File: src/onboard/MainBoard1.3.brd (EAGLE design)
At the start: 134.6 x 80.5 mm, 86 parts, among them IC1 MIC29310-5.0BT, IC3 A5975D, U1 ADAFRUIT_BMP280_BAROMETER

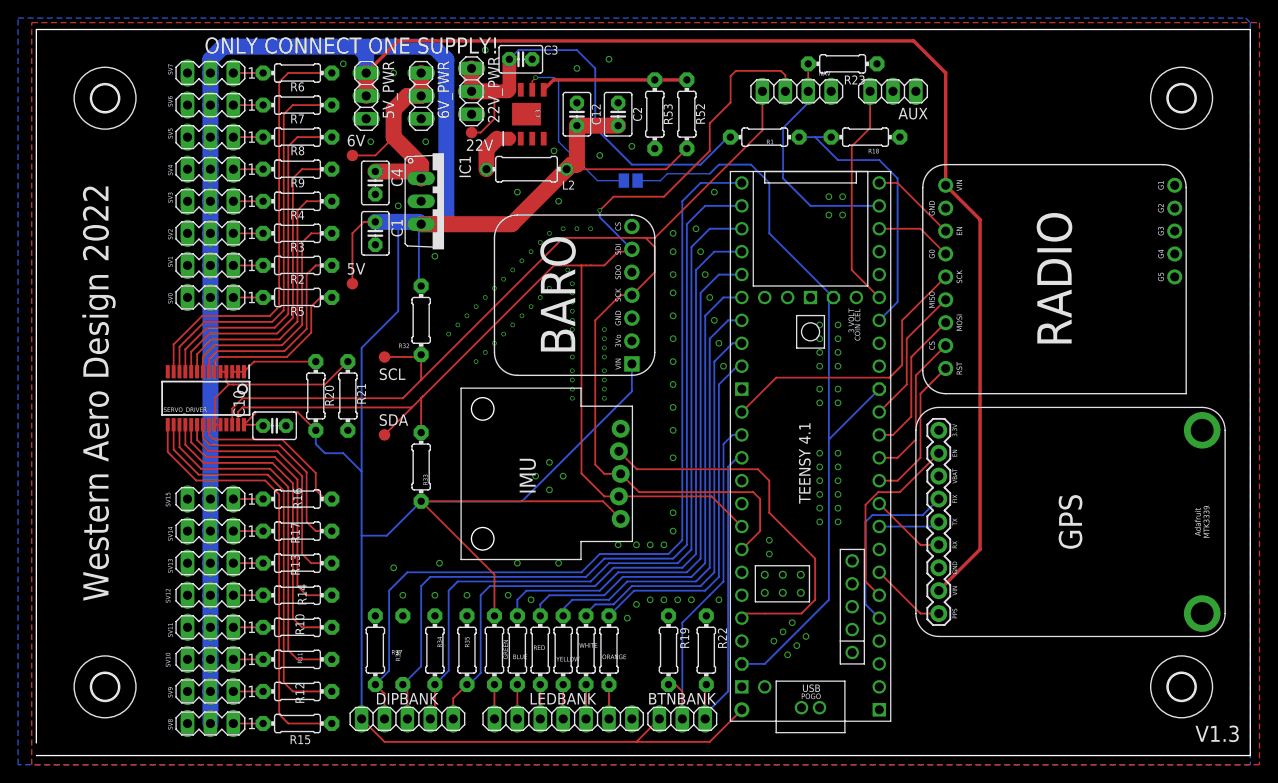
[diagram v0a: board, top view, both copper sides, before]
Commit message: Renamed main board files
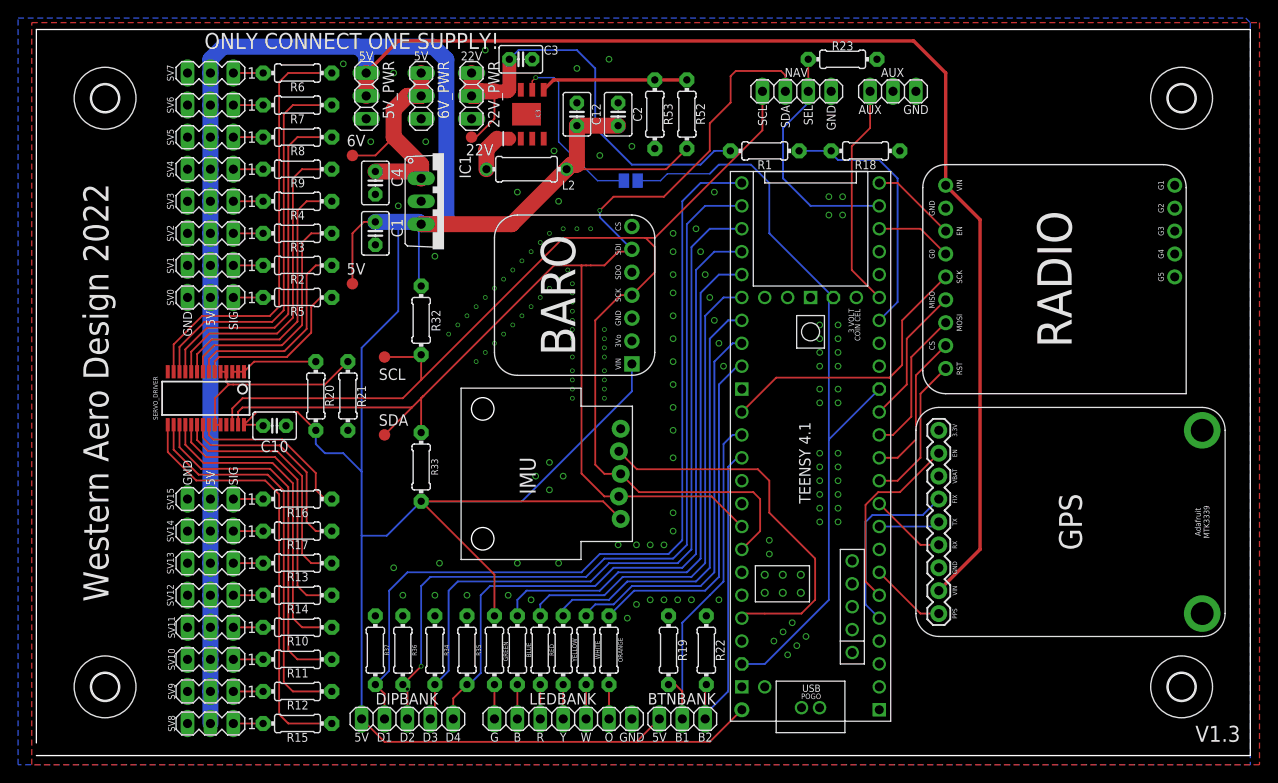
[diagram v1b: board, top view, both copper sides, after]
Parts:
- moved R1 1.52 mm to (80.8, 67.1)
- moved R18 1.52 mm to (91.9, 67.1)
- moved 22V 0.51 mm to (48.3, 68.6)
- moved 22V_PWR 0.51 mm to (48.3, 73.2)
- moved R23 0.51 mm to (89.4, 77.2)
- flipped R36 to the top
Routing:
- net BATLEVEL: track 31.2 -> 28.9 mm
- net SELECT_PIN: track 25.8 -> 26.3 mm
- net DIP2: vias 0 -> 2
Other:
- board text added: "22V"
- board text added: "5V"
- board text added: "AUX"
- board text added: "B"
- board text added: "B1"
- board text added: "B2"
- board text added: "D1"
- board text added: "D2"
- board text added: "D3"
- board text added: "D4"
- board text added: "G"
- board text added: "GND"
- board text added: "O"
- board text added: "R"
- board text added: "SCL"
- board text added: "SDA"
- board text added: "SEL"
- board text added: "SIG"
- board text added: "W"
- board text added: "Y"

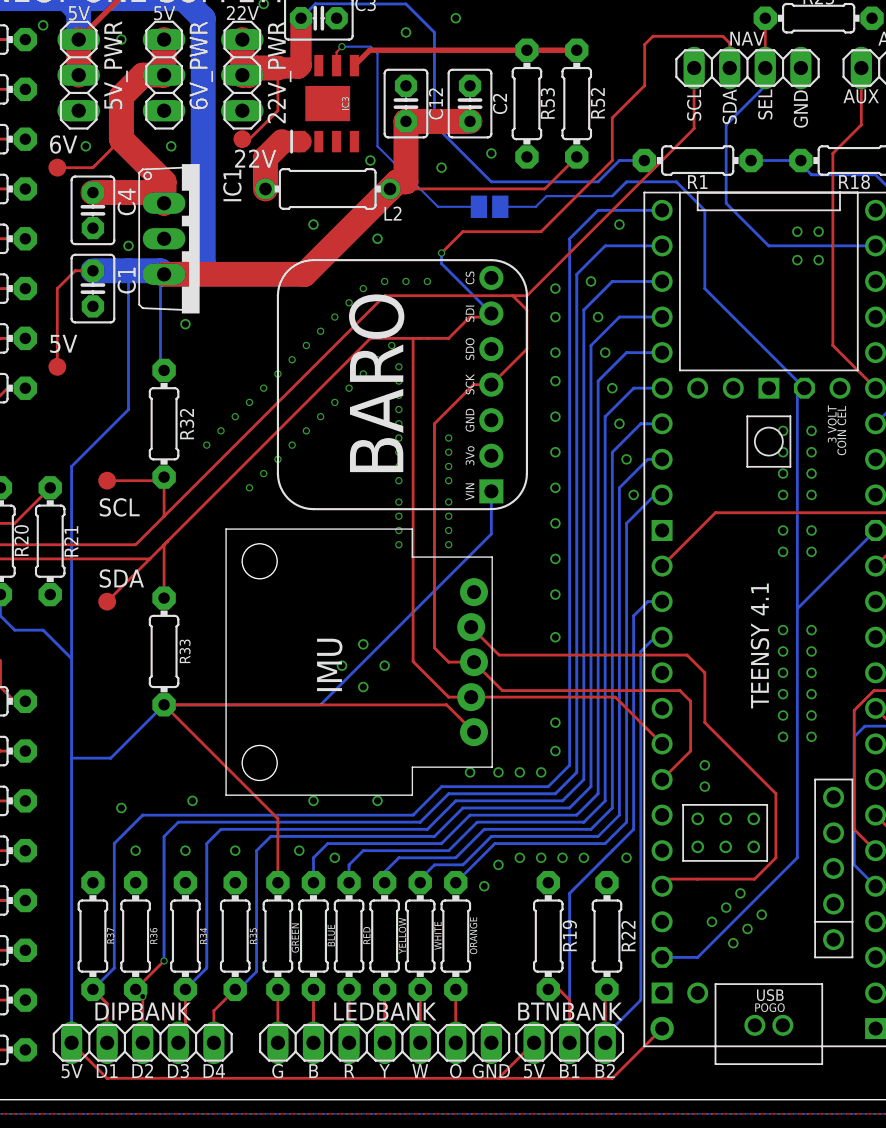
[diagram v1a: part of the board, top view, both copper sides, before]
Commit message: Added gnd test point
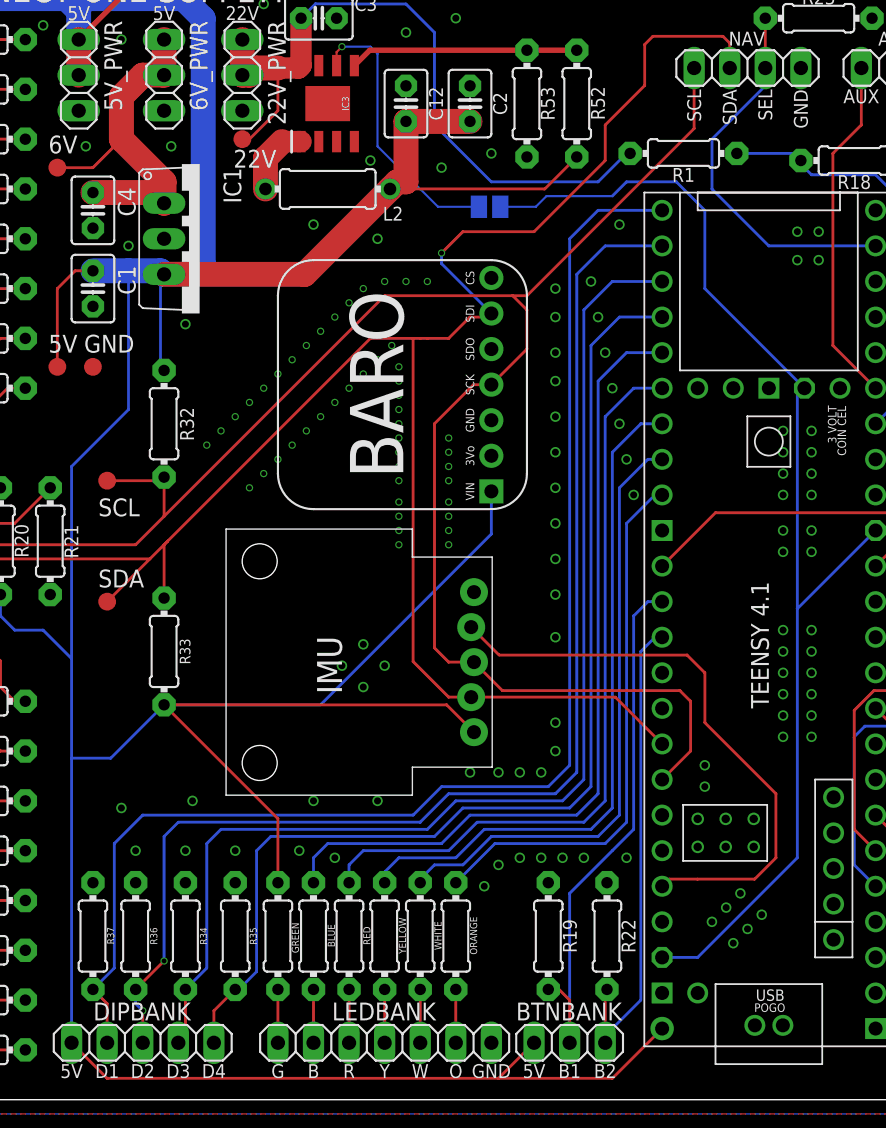
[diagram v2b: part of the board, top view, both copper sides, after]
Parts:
- added GND: PTR1B1,27, testpad:B1,27
- moved R1 1.14 mm to (79.8, 67.6)
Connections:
- net GND: now also GND.TP
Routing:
- net BATLEVEL: track 28.9 -> 30.1 mm
- net SELECT_PIN: track 26.3 -> 27.1 mm
- net 22V_INPUT: track 51.5 -> 50.7 mm
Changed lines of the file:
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@@
 <attribute name="VALUE" x="56.261" y="76.708" size="0.9906" layer="27" ratio="10" align="center-left"/>
 </element>
-<element name="R1" library="adafruit" library_urn="urn:adsk.eagle:library:420" package="0204/7" package3d_urn="urn:adsk.eagle:package:6240596/1" value="1.8M" x="80.772" y="67.056" smashed="yes" rot="R180">
-<attribute name="NAME" x="80.772" y="66.0146" size="0.9906" layer="25" ratio="12" rot="R180" align="bottom-center"/>
-<attribute name="VALUE" x="80.7466" y="67.0306" size="0.9906" layer="27" ratio="12" rot="R180" align="center"/>
+<element name="R1" library="adafruit" library_urn="urn:adsk.eagle:library:420" package="0204/7" package3d_urn="urn:adsk.eagle:package:6240596/1" value="1.8M" x="79.756" y="67.564" smashed="yes" rot="R180">
+<attribute name="NAME" x="79.756" y="66.5226" size="0.9906" layer="25" ratio="12" rot="R180" align="bottom-center"/>
+<attribute name="VALUE" x="79.7306" y="67.5386" size="0.9906" layer="27" ratio="12" rot="R180" align="center"/>
 </element>
 <element name="R18" library="adafruit" library_urn="urn:adsk.eagle:library:420" package="0204/7" package3d_urn="urn:adsk.eagle:package:6240596/1" value="430k" x="91.948" y="67.056" smashed="yes" rot="R180">
@@
 <attribute name="POPULARITY" value="33" x="65.913" y="63.754" size="1.778" layer="28" rot="MR180" display="off"/>
 <attribute name="VALUE" x="66.3131" y="63.754" size="0.02" layer="28" rot="MR180"/>
+</element>
+<element name="GND" library="testpad" library_urn="urn:adsk.eagle:library:385" package="B1,27" package3d_urn="urn:adsk.eagle:package:27944/2" value="PTR1B1,27" x="37.592" y="52.324" smashed="yes">
+<attribute name="NAME" x="36.957" y="53.34" size="1.27" layer="25" ratio="10"/>
+<attribute name="POPULARITY" value="2" x="37.592" y="52.324" size="1.778" layer="27" display="off"/>
+<attribute name="TP_SIGNAL_NAME" value="" x="37.592" y="52.324" size="1.778" layer="27" display="off"/>
+<attribute name="VALUE" x="36.957" y="51.562" size="0.0254" layer="27"/>
 </element>
 </elements>
@@
 <wire x1="82.5754" y1="75.9206" x2="77.567675" y2="75.9206" width="0.2032" layer="1"/>
 <wire x1="76.9874" y1="75.340325" x2="76.9874" y2="72.4154" width="0.2032" layer="1"/>
-<wire x1="74.676" y1="70.104" x2="74.676" y2="67.056" width="0.2032" layer="1"/>
-<wire x1="74.676" y1="67.056" x2="69.596" y2="61.976" width="0.2032" layer="1"/>
+<wire x1="74.168" y1="69.596" x2="74.168" y2="67.056" width="0.2032" layer="1"/>
+<wire x1="74.168" y1="67.056" x2="69.088" y2="61.976" width="0.2032" layer="1"/>
 <wire x1="64.008" y1="61.976" x2="62.484" y2="60.452" width="0.2032" layer="1"/>
 <via x="62.484" y="60.452" extent="1-16" drill="0.35"/>
 <wire x1="62.484" y1="60.452" x2="62.484" y2="59.69" width="0.2032" layer="16"/>
 <wire x1="62.484" y1="59.69" x2="66.04" y2="56.134" width="0.2032" layer="16"/>
-<wire x1="76.9874" y1="72.4154" x2="74.676" y2="70.104" width="0.2032" layer="1"/>
-<wire x1="69.596" y1="61.976" x2="64.008" y2="61.976" width="0.2032" layer="1"/>
+<wire x1="76.9874" y1="72.4154" x2="74.168" y2="69.596" width="0.2032" layer="1"/>
+<wire x1="69.088" y1="61.976" x2="64.008" y2="61.976" width="0.2032" layer="1"/>
 <wire x1="64.599" y1="28.742" x2="62.992" y2="28.742" width="0.2032" layer="1"/>
 <wire x1="62.992" y1="28.742" x2="60.452" y2="31.282" width="0.2032" layer="1"/>
@@
 <contactref element="R36" pad="2"/>
 <contactref element="DIPBANK" pad="3"/>
-<wire x1="40.64" y1="7.874" x2="41.148" y2="7.366" width="0.2032" layer="16"/>
-<wire x1="41.148" y1="7.366" x2="41.148" y2="4.064" width="0.2032" layer="1"/>
+<wire x1="40.64" y1="7.874" x2="40.64" y2="6.858" width="0.2032" layer="16"/>
+<wire x1="41.148" y1="6.35" x2="40.64" y2="6.858" width="0.2032" layer="16"/>
+<wire x1="41.148" y1="6.35" x2="41.148" y2="4.064" width="0.2032" layer="1"/>
 <wire x1="74.168" y1="60.96" x2="72.136" y2="58.928" width="0.2032" layer="16"/>
 <wire x1="78.232" y1="60.96" x2="74.168" y2="60.96" width="0.2032" layer="16"/>
@@
 <wire x1="42.672" y1="9.906" x2="40.64" y2="7.874" width="0.2032" layer="1"/>
 <wire x1="42.672" y1="18.796" x2="42.672" y2="9.906" width="0.2032" layer="16"/>
-<via x="41.148" y="7.366" extent="1-16" drill="0.35"/>
+<via x="41.148" y="6.35" extent="1-16" drill="0.35"/>
 <via x="42.672" y="9.906" extent="1-16" drill="0.35"/>
 </signal>
@@
 <via x="44.196" y="55.372" extent="1-16" drill="0.5"/>
 <via x="34.036" y="76.708" extent="1-16" drill="0.5"/>
+<contactref element="GND" pad="TP"/>
 </signal>
 <signal name="GPS_EN">
@@
 <contactref element="TEENSY4.1" pad="31-CTX3"/>
 <wire x1="85.598" y1="73.66" x2="85.598" y2="72.39" width="0.2032" layer="16"/>
-<wire x1="85.598" y1="72.39" x2="82.804" y2="69.596" width="0.2032" layer="16"/>
-<wire x1="82.804" y1="69.596" x2="82.804" y2="64.008" width="0.2032" layer="16"/>
+<wire x1="85.598" y1="72.39" x2="81.788" y2="68.58" width="0.2032" layer="16"/>
+<wire x1="81.788" y1="68.58" x2="81.788" y2="65.024" width="0.2032" layer="16"/>
 <wire x1="85.852" y1="60.96" x2="93.472" y2="60.96" width="0.2032" layer="16"/>
-<wire x1="82.804" y1="64.008" x2="85.852" y2="60.96" width="0.2032" layer="16"/>
+<wire x1="81.788" y1="65.024" x2="85.852" y2="60.96" width="0.2032" layer="16"/>
 <wire x1="85.598" y1="77.216" x2="85.598" y2="73.66" width="0.2032" layer="1"/>
 </signal>
@@
 <wire x1="88.9" y1="66.04" x2="88.138" y2="66.802" width="0.2032" layer="16"/>
 <wire x1="88.138" y1="66.802" x2="88.138" y2="67.056" width="0.2032" layer="16"/>
-<wire x1="84.582" y1="67.056" x2="88.138" y2="67.056" width="0.2032" layer="16"/>
+<wire x1="87.63" y1="67.564" x2="83.566" y2="67.564" width="0.2032" layer="16"/>
+<wire x1="87.63" y1="67.564" x2="88.138" y2="67.056" width="0.2032" layer="16"/>
 </signal>
 <signal name="MISO0">
@@
 <wire x1="66.04" y1="65.532" x2="73.66" y2="65.532" width="0.2032" layer="16"/>
 <contactref element="R1" pad="2"/>
-<wire x1="76.962" y1="67.056" x2="75.184" y2="67.056" width="0.2032" layer="16"/>
-<wire x1="75.184" y1="67.056" x2="73.66" y2="65.532" width="0.2032" layer="16"/>
+<wire x1="75.946" y1="67.564" x2="75.692" y2="67.564" width="0.2032" layer="16"/>
+<wire x1="75.692" y1="67.564" x2="73.66" y2="65.532" width="0.2032" layer="16"/>
 <wire x1="48.26" y1="68.58" x2="48.768" y2="68.58" width="0.2032" layer="1"/>
 <wire x1="48.768" y1="68.58" x2="50.8" y2="70.612" width="0.2032" layer="1"/>

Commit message: Performed ERC and made changes
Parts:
- 22V_PWR: value (none) -> 22V_PWR
- 5V_PWR: value (none) -> 5V_PWR
- 6V_PWR: value (none) -> 6V_PWR
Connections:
- removed net AUX_DATA: TEENSY4.1.6-OUT1D
- removed net N$4: AUX.2
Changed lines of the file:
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@@
 <attribute name="VALUE" x="47.498" y="7.239" size="1.27" layer="27" rot="R180"/>
 </element>
-<element name="6V_PWR" library="pinhead" library_urn="urn:adsk.eagle:library:325" package="1X03" package3d_urn="urn:adsk.eagle:package:22458/2" value="" x="42.672" y="73.152" smashed="yes" rot="R270">
+<element name="6V_PWR" library="pinhead" library_urn="urn:adsk.eagle:library:325" package="1X03" package3d_urn="urn:adsk.eagle:package:22458/2" value="6V_PWR" x="42.672" y="73.152" smashed="yes" rot="R270">
 <attribute name="NAME" x="44.5008" y="77.0382" size="1.27" layer="25" ratio="10" rot="R270"/>
 <attribute name="POPULARITY" value="92" x="42.672" y="73.152" size="1.778" layer="27" rot="R270" display="off"/>
-<attribute name="VALUE" x="39.497" y="76.962" size="1.27" layer="27" rot="R270"/>
 </element>
 <element name="LEDBANK" library="pinhead" library_urn="urn:adsk.eagle:library:325" package="1X07" package3d_urn="urn:adsk.eagle:package:22477/2" value="" x="58.42" y="4.064" smashed="yes" rot="R180">
@@
 <attribute name="VALUE" x="67.31" y="7.239" size="1.27" layer="27" rot="R180"/>
 </element>
-<element name="22V_PWR" library="pinhead" library_urn="urn:adsk.eagle:library:325" package="1X03" package3d_urn="urn:adsk.eagle:package:22458/2" value="" x="48.26" y="73.152" smashed="yes" rot="R270">
+<element name="22V_PWR" library="pinhead" library_urn="urn:adsk.eagle:library:325" package="1X03" package3d_urn="urn:adsk.eagle:package:22458/2" value="22V_PWR" x="48.26" y="73.152" smashed="yes" rot="R270">
 <attribute name="NAME" x="50.0888" y="77.0382" size="1.27" layer="25" ratio="10" rot="R270"/>
 <attribute name="POPULARITY" value="92" x="48.26" y="73.152" size="1.778" layer="27" rot="R270" display="off"/>
-<attribute name="VALUE" x="45.085" y="76.962" size="1.27" layer="27" rot="R270"/>
 </element>
 <element name="5V" library="testpad" library_urn="urn:adsk.eagle:library:385" package="B1,27" package3d_urn="urn:adsk.eagle:package:27944/2" value="PTR1B1,27" x="35.052" y="52.324" smashed="yes">
@@
 <attribute name="VALUE" x="34.417" y="65.786" size="0.0254" layer="27"/>
 </element>
-<element name="5V_PWR" library="pinhead" library_urn="urn:adsk.eagle:library:325" package="1X03" package3d_urn="urn:adsk.eagle:package:22458/2" value="" x="36.576" y="73.152" smashed="yes" rot="R270">
+<element name="5V_PWR" library="pinhead" library_urn="urn:adsk.eagle:library:325" package="1X03" package3d_urn="urn:adsk.eagle:package:22458/2" value="5V_PWR" x="36.576" y="73.152" smashed="yes" rot="R270">
 <attribute name="NAME" x="38.4048" y="77.0382" size="1.27" layer="25" ratio="10" rot="R270"/>
 <attribute name="POPULARITY" value="92" x="36.576" y="73.152" size="1.778" layer="27" rot="R270" display="off"/>
-<attribute name="VALUE" x="33.401" y="76.962" size="1.27" layer="27" rot="R270"/>
 </element>
 <element name="IC1" library="linear" library_urn="urn:adsk.eagle:library:262" package="TO220V" package3d_urn="urn:adsk.eagle:package:16417/2" value="MIC29310-5.0BT" x="45.212" y="61.468" smashed="yes" rot="R270">
@@
 <contactref element="SV11" pad="3"/>
 <contactref element="SV9" pad="3"/>
-<contactref element="TEENSY4.1" pad="GND1"/>
-<contactref element="TEENSY4.1" pad="GND3"/>
 <contactref element="R53" pad="1"/>
 <contactref element="C12" pad="2"/>
 <contactref element="SERVO_DRIVER" pad="14"/>
-<contactref element="TEENSY4.1" pad="GND6"/>
 <contactref element="NAV" pad="1"/>
 <contactref element="C3" pad="2"/>
@@
 <contactref element="R19" pad="1"/>
 <contactref element="R22" pad="1"/>
-<contactref element="TEENSY4.1" pad="GND2"/>
-<contactref element="TEENSY4.1" pad="GND4"/>
-<contactref element="TEENSY4.1" pad="GND5"/>
 <contactref element="6V_PWR" pad="3"/>
 <contactref element="LEDBANK" pad="1"/>
@@
 <via x="34.036" y="76.708" extent="1-16" drill="0.5"/>
 <contactref element="GND" pad="TP"/>
+<contactref element="TEENSY4.1" pad="GND1"/>
+<contactref element="TEENSY4.1" pad="GND2"/>
+<contactref element="TEENSY4.1" pad="GND3"/>
+<contactref element="TEENSY4.1" pad="GND4"/>
+<contactref element="TEENSY4.1" pad="GND5"/>
+<contactref element="TEENSY4.1" pad="GND6"/>
 </signal>
 <signal name="GPS_EN">
@@
 <signal name="PWM13">
 <contactref element="SERVO_DRIVER" pad="20"/>
-<contactref element="R13" pad="1"/>
 <wire x1="17.821" y1="36.686" x2="17.821" y2="35.0036125" width="0.2032" layer="1"/>
 <wire x1="17.821" y1="35.0036125" x2="19.0726125" y2="33.752" width="0.2032" layer="1"/>
@@
 <wire x1="29.464" y1="31.01225" x2="29.464" y2="22.352" width="0.2032" layer="1"/>
 <wire x1="29.464" y1="22.352" x2="30.48" y2="21.336" width="0.2032" layer="1"/>
+<wire x1="26.72425" y1="33.752" x2="29.464" y2="31.01225" width="0.2032" layer="1"/>
+<contactref element="R13" pad="1"/>
 <wire x1="30.48" y1="21.336" x2="32.766" y2="21.336" width="0.2032" layer="1"/>
-<wire x1="26.72425" y1="33.752" x2="29.464" y2="31.01225" width="0.2032" layer="1"/>
 </signal>
 <signal name="PWM12">
 <contactref element="SERVO_DRIVER" pad="19"/>
-<contactref element="R14" pad="1"/>
 <wire x1="17.171" y1="36.686" x2="17.171" y2="34.73436875" width="0.2032" layer="1"/>
 <wire x1="17.171" y1="34.73436875" x2="18.80336875" y2="33.102" width="0.2032" layer="1"/>
@@
 <wire x1="28.956" y1="30.601" x2="28.956" y2="18.796" width="0.2032" layer="1"/>
 <wire x1="28.956" y1="18.796" x2="29.972" y2="17.78" width="0.2032" layer="1"/>
+<wire x1="26.455" y1="33.102" x2="28.956" y2="30.601" width="0.2032" layer="1"/>
+<contactref element="R14" pad="1"/>
 <wire x1="29.972" y1="17.78" x2="32.766" y2="17.78" width="0.2032" layer="1"/>
-<wire x1="26.455" y1="33.102" x2="28.956" y2="30.601" width="0.2032" layer="1"/>
 </signal>
 <signal name="PWM11">
@@
 <wire x1="57.359" y1="74.93" x2="68.58" y2="74.93" width="0.381" layer="1"/>
 <wire x1="68.58" y1="74.93" x2="72.136" y2="74.93" width="0.381" layer="1"/>
-</signal>
-<signal name="AUX_DATA">
-<contactref element="TEENSY4.1" pad="6-OUT1D"/>
 </signal>
 <signal name="SELECT_PIN">
@@
 <wire x1="37.592" y1="66.548" x2="39.624" y2="68.58" width="0.2032" layer="1"/>
 </signal>
-<signal name="N$4">
-<contactref element="AUX" pad="2"/>
-</signal>
 <signal name="AUX">

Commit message: Updated BMP 280 VIN pin to be IO
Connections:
- net GND: now also C1.2
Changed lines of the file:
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@@
 <contactref element="TEENSY4.1" pad="GND5"/>
 <contactref element="TEENSY4.1" pad="GND6"/>
+<contactref element="C1" pad="2"/>
 </signal>
 <signal name="GPS_EN">
